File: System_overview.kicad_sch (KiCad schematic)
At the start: 0 parts

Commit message: creating hierarchy
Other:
- note added: "END OF TRAVEL SWITCHES"
- note removed: "END OF TRAVEL"
- note removed: "EXTERNAL EQUIPMENT"
- note removed: "EXTERNAL LOAD / MECHANICS"
- note removed: "LOWER"
- note removed: "NO / NC and wiring: TBD"
- note removed: "Reed contacts"
- note removed: "Shared return shown"
- note removed: "UPPER"
- note removed: "Upper / lower reed switches"
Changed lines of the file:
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@@
 		)
 	)
-	(polyline
-		(pts
-			(xy 49.82 131.14) (xy 57.82 131.14) (xy 57.82 115.98) (xy 109.82 115.98)
-		)
-		(stroke
-			(width 0.25)
-			(type default)
-		)
-		(fill
-			(type none)
-		)
-	)
-	(polyline
-		(pts
-			(xy 23.82 128.14) (xy 45.82 128.14) (xy 45.82 134.14) (xy 23.82 134.14) (xy 23.82 128.14)
-		)
-		(stroke
-			(width 0.18)
-			(type default)
-		)
-		(fill
-			(type none)
-		)
-	)
-	(polyline
-		(pts
-			(xy 23.82 141.14) (xy 45.82 141.14) (xy 45.82 147.14) (xy 23.82 147.14) (xy 23.82 141.14)
-		)
-		(stroke
-			(width 0.18)
-			(type default)
-		)
-		(fill
-			(type none)
-		)
-	)
-	(polyline
-		(pts
-			(xy 49.82 144.14) (xy 70.82 144.14) (xy 70.82 126.14) (xy 109.82 126.14)
-		)
-		(stroke
-			(width 0.25)
+	(rectangle
+		(start 38.1 127)
+		(end 63.5 152.4)
+		(stroke
+			(width 0)
 			(type default)
 		)
@@
 	)
 	(rectangle
+		(start 25.4 114.3)
+		(end 76.2 165.1)
+		(stroke
+			(width 0)
+			(type dash)
+		)
+		(fill
+			(type none)
+		)
+	)
+	(rectangle
 		(start 223.52 154.94)
 		(end 224.79 160.02)
@@
 		)
 	)
-	(polyline
-		(pts
-			(xy 18.82 131.14) (xy 18.82 152.14) (xy 64.82 152.14) (xy 64.82 136.3) (xy 109.82 136.3)
-		)
-		(stroke
-			(width 0.25)
-			(type default)
-		)
-		(fill
-			(type none)
-		)
-	)
 	(rectangle
 		(start 257.81 154.94)
@@
 		)
 	)
-	(polyline
-		(pts
-			(xy 14.82 109.14) (xy 76.82 109.14) (xy 76.82 158.14) (xy 14.82 158.14) (xy 14.82 109.14)
-		)
-		(stroke
-			(width 0.25)
-			(type dash)
-		)
-		(fill
-			(type none)
-		)
-	)
 	(rectangle
 		(start 38.1 63.5)
@@
 		)
 	)
-	(polyline
-		(pts
-			(xy 241.3 90.17) (xy 241.3 95.25)
-		)
-		(stroke
-			(width 0.254)
-			(type solid)
-			(color 0 0 0 1)
-		)
-		(fill
-			(type none)
-		)
-	)
 	(rectangle
 		(start 215.9 139.7)
@@
 		)
 	)
-	(text "END OF TRAVEL"
-		(exclude_from_sim no)
-		(at 18.82 115.14 0)
-		(effects
-			(font
-				(size 1.6 1.6)
-				(bold yes)
-			)
-			(justify left)
-		)
-	)
 	(text "DESK MECHANISM"
 		(exclude_from_sim no)
@@
 		)
 	)
-	(text "UPPER"
-		(exclude_from_sim no)
-		(at 24.82 137.14 0)
-		(effects
-			(font
-				(size 1 1)
-			)
-			(justify left)
-		)
-	)
 	(text "19.5 V, 3 A"
 		(exclude_from_sim no)
@@
 		)
 	)
-	(text "NO / NC and wiring: TBD"
-		(exclude_from_sim no)
-		(at 20.82 155.14 0)
-		(effects
-			(font
-				(size 1.05 1.05)
-			)
-			(justify left)
-		)
-	)
 	(text "Control input / logic"
 		(exclude_from_sim no)
@@
 		)
 	)
-	(text "LOWER"
-		(exclude_from_sim no)
-		(at 24.82 150.14 0)
-		(effects
-			(font
-				(size 1 1)
-			)
-			(justify left)
-		)
-	)
 	(text "DC POWER SUPPLY"
 		(exclude_from_sim no)
@@
 		)
 	)
-	(text "EXTERNAL EQUIPMENT"
-		(exclude_from_sim no)
-		(at 14.82 42.14 0)
-		(effects
-			(font
-				(size 1.5 1.5)
-				(bold yes)
-			)
-			(justify left)
-		)
-	)
-	(text "Reed contacts"
-		(exclude_from_sim no)
-		(at 80.82 109.14 0)
-		(effects
-			(font
-				(size 1.15 1.15)
-			)
-			(justify left)
-		)
-	)
-	(text "EXTERNAL LOAD / MECHANICS"
-		(exclude_from_sim no)
-		(at 217.82 42.14 0)
-		(effects
-			(font
-				(size 1.5 1.5)
-				(bold yes)
-			)
-			(justify left)
-		)
-	)
-	(text "Shared return shown"
-		(exclude_from_sim no)
-		(at 79.82 143.14 0)
-		(effects
-			(font
-				(size 1 1)
-			)
-			(justify left)
+	(text "END OF TRAVEL SWITCHES"
+		(exclude_from_sim no)
+		(at 26.035 115.57 0)
+		(effects
+			(font
+				(size 1.524 1.524)
+				(thickness 0.1905)
+			)
+			(justify left top)
 		)
 	)
@@
 			(font
 				(size 1.016 1.016)
-			)
-			(justify left)
-		)
-	)
-	(text "Upper / lower reed switches"
-		(exclude_from_sim no)
-		(at 18.82 121.14 0)
-		(effects
-			(font
-				(size 1.2 1.2)
 			)
 			(justify left)
@@
 	(polyline
 		(pts
-			(xy 18.82 144.14) (xy 28.82 144.14)
-		)
-		(stroke
-			(width 0.25)
-			(type default)
-		)
-	)
-	(polyline
-		(pts
-			(xy 28.82 131.14) (xy 38.82 129.64)
-		)
-		(stroke
-			(width 0.25)
-			(type default)
+			(xy 104.14 116.84) (xy 114.3 116.84)
+		)
+		(stroke
+			(width 0)
+			(type solid)
+			(color 0 0 0 1)
+		)
+	)
+	(polyline
+		(pts
+			(xy 63.5 134.62) (xy 99.06 134.62)
+		)
+		(stroke
+			(width 0)
+			(type solid)
+			(color 0 0 0 1)
 		)
 	)
@@
 	(polyline
 		(pts
-			(xy 18.82 131.14) (xy 28.82 131.14)
-		)
-		(stroke
-			(width 0.25)
-			(type default)
-		)
-	)
-	(polyline
-		(pts
 			(xy 262.89 154.94) (xy 264.16 153.67)
 		)
@@
 	(polyline
 		(pts
-			(xy 39.82 144.14) (xy 49.82 144.14)
-		)
-		(stroke
-			(width 0.25)
-			(type default)
+			(xy 63.5 139.7) (xy 104.14 139.7)
+		)
+		(stroke
+			(width 0)
+			(type solid)
+			(color 0 0 0 1)
+		)
+	)
+	(polyline
+		(pts
+			(xy 99.06 134.62) (xy 99.06 111.76)
+		)
+		(stroke
+			(width 0)
+			(type solid)
+			(color 0 0 0 1)
 		)
 	)
@@
 	(polyline
 		(pts
+			(xy 104.14 139.7) (xy 104.14 116.84)
+		)
+		(stroke
+			(width 0)
+			(type solid)
+			(color 0 0 0 1)
+		)
+	)
+	(polyline
+		(pts
 			(xy 262.89 154.94) (xy 269.24 154.94)
 		)
@@
 	(polyline
 		(pts
+			(xy 101.6 137.16) (xy 101.6 114.3)
+		)
+		(stroke
+			(width 0)
+			(type solid)
+			(color 0 0 0 1)
+		)
+	)
+	(polyline
+		(pts
 			(xy 210.82 78.74) (xy 210.82 100.33)
 		)
@@
 	(polyline
 		(pts
+			(xy 63.5 137.16) (xy 101.6 137.16)
+		)
+		(stroke
+			(width 0)
+			(type solid)
+			(color 0 0 0 1)
+		)
+	)
+	(polyline
+		(pts
 			(xy 220.98 160.02) (xy 227.33 160.02)
 		)
@@
 	(polyline
 		(pts
+			(xy 99.06 111.76) (xy 114.3 111.76)
+		)
+		(stroke
+			(width 0)
+			(type solid)
+			(color 0 0 0 1)
+		)
+	)
+	(polyline
+		(pts
 			(xy 262.89 77.47) (xy 269.24 77.47)
 		)
@@
 	(polyline
 		(pts
-			(xy 18.82 144.14) (xy 18.82 152.14)
-		)
-		(stroke
-			(width 0.25)
-			(type default)
-		)
-	)
-	(polyline
-		(pts
 			(xy 177.8 100.33) (xy 210.82 100.33)
 		)
@@
 	(polyline
 		(pts
-			(xy 39.82 131.14) (xy 49.82 131.14)
-		)
-		(stroke
-			(width 0.25)
-			(type default)
-		)
-	)
-	(polyline
-		(pts
 			(xy 262.89 154.94) (xy 264.16 156.21)
 		)
@@
 	(polyline
 		(pts
+			(xy 101.6 114.3) (xy 114.3 114.3)
+		)
+		(stroke
+			(width 0)
+			(type solid)
+			(color 0 0 0 1)
+		)
+	)
+	(polyline
+		(pts
 			(xy 177.8 105.41) (xy 228.6 105.41)
 		)
@@
 	(polyline
 		(pts
-			(xy 28.82 144.14) (xy 38.82 142.64)
-		)
-		(stroke
-			(width 0.25)
-			(type default)
-		)
-	)
+			(xy 241.3 90.17) (xy 241.3 95.25)
+		)
+		(stroke
+			(width 0.254)
+			(type solid)
+			(color 0 0 0 1)
+		)
+	)

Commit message: testing links
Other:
- note added: "Return to front sheet"
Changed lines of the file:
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@@
+		)
+	)
+	(text "Return to front sheet"
+		(exclude_from_sim no)
+		(at 12.7 197.485 0)
+		(effects
+			(font
+				(face "DejaVu Sans")
+				(size 2.032 2.032)
+				(thickness 0.3175)
+				(color 0 0 0 1)
+			)
+			(justify left bottom)
+			(href "#1")
 		)
 	)

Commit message: system overview and interfaces done
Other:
- sheet Block_diagram renamed Block diagram
- added sheet DC power supply (Interface_Power_supply.kicad_sch)
- added sheet Limit switches (Interface_Limit_switches.kicad_sch)
- added sheet Servomotor (Interface_servomotor.kicad_sch)
- note added: "${SHEETNAME}"
- note added: "Bottom"
- note added: "Control logic HMI Motor driver Encoder interface Limit switch interface"
- note added: "Motor, gearbox and encoder"
- note added: "This sheet shows the overall system and the interfaces to external components. External components are shown for system context only and are not part of this schematic. Only the "DESIGNED SUBSYSTEM" is covered by this schematic."
- note added: "Top"
- note removed: "19.5 V, 3 A"
- note removed: "Control input / logic"
- note removed: "DC POWER SUPPLY"
- note removed: "END OF TRAVEL SWITCHES"
- note removed: "Encoder GND"
- note removed: "Encoder decoding"
- note removed: "Encoder signal A"
- note removed: "Encoder signal B"
- note removed: "Encoder supply"
- note removed: "End-switch inputs"
- note removed: "GND"
- note removed: "Integrated encoder"
- note removed: "Motor / gearbox"
- note removed: "Motor A"
- note removed: "Motor B"
- note removed: "Motor power stage"
- note removed: "S24"
- note removed: "SERVOMOTOR PACKAGE"
- note removed: "STANDING DESK / SYSTEM OVERVIEW"

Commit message: testing green mask
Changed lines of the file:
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@@
 			(width 0)
 			(type dash)
+			(color 0 0 0 1)
 		)
 		(fill
@@
 	(text "This sheet shows the overall system and the interfaces to external components.\nExternal components are shown for system context only and are not part of this schematic.\nOnly the \"DESIGNED SUBSYSTEM\" is covered by this schematic."
 		(exclude_from_sim no)
-		(at 25.4 165.1 0)
+		(at 38.1 166.37 0)
 		(effects
 			(font
-				(size 1.27 1.27)
+				(size 2.032 2.032)
+				(color 194 0 0 1)
 			)
 			(justify left top)
@@
 			(font
 				(size 1.27 1.27)
+				(color 0 0 0 1)
 			)
 		)
@@
 				(size 1.524 1.524)
 				(thickness 0.1905)
+				(bold yes)
+				(color 255 0 0 1)
 			)
 			(justify left top)
@@
 	(text "${SHEETNAME}"
 		(exclude_from_sim no)
-		(at 283.21 13.97 0)
+		(at 283.21 14.605 0)
 		(effects
 			(font
-				(size 2.54 2.54)
+				(face "DejaVu Sans")
+				(size 3.81 3.81)
 				(bold yes)
+				(color 0 0 0 1)
 			)
 			(justify right top)

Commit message: reorganised sch and pcb
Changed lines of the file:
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@@
 			(font
 				(size 2.032 2.032)
-				(color 194 0 0 1)
+				(color 0 0 0 1)
 			)
 			(justify left top)
@@
 		(effects
 			(font
-				(size 1.27 1.27)
+				(size 1.524 1.524)
 				(color 0 0 0 1)
 			)
@@
 	(text "DESIGNED SUBSYSTEM"
 		(exclude_from_sim no)
-		(at 128.27 40.005 0)
+		(at 151.765 42.545 0)
 		(effects
 			(font
 				(face "DejaVu Sans")
-				(size 1.524 1.524)
+				(size 2.032 2.032)
 				(thickness 0.1905)
 				(bold yes)
-				(color 255 0 0 1)
-			)
-			(justify left top)
+				(color 0 0 0 1)
+			)
+			(justify top)
 		)
 	)
@@
 		)
 		(fill
-			(color 194 194 194 1)
+			(color 250 240 240 1)
 		)
 		(property "Sheetname" "Servomotor"
@@
 		)
 		(fill
-			(color 194 194 194 1)
+			(color 250 240 240 1)
 		)
 		(property "Sheetname" "DC power supply"
@@
 		)
 		(fill
-			(color 194 194 194 1)
+			(color 250 240 240 1)
 		)
 		(property "Sheetname" "Limit switches"

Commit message: updated sch template (A4)
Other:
- note removed: "${SHEETNAME}"
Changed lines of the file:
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@@
-		)
-	)
-	(text "${SHEETNAME}"
-		(exclude_from_sim no)
-		(at 283.21 14.605 0)
-		(effects
-			(font
-				(face "DejaVu Sans")
-				(size 3.81 3.81)
-				(bold yes)
-				(color 0 0 0 1)
-			)
-			(justify right top)
 		)
 	)
@@
 				(size 2.032 2.032)
 				(thickness 0.3175)
-				(color 0 0 0 1)
+				(color 0 0 194 1)
 			)
 			(justify left bottom)

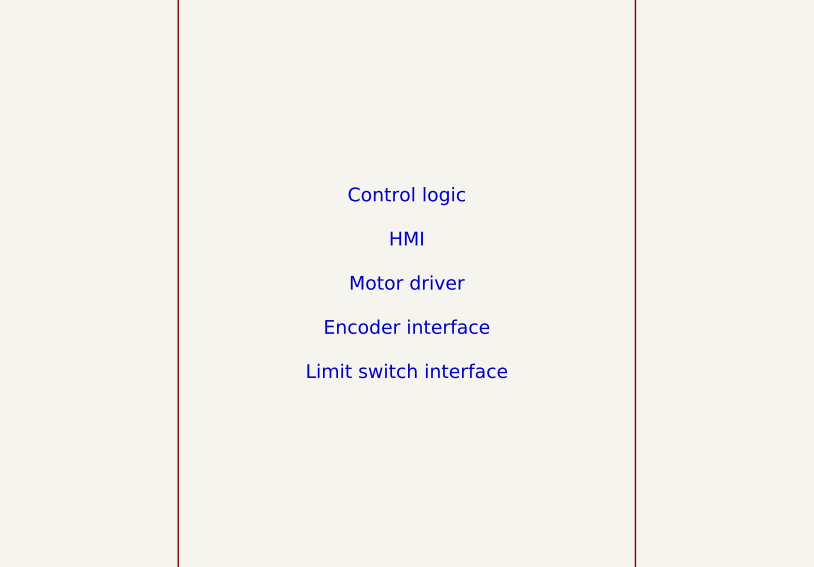
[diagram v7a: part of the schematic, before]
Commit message: new sch size
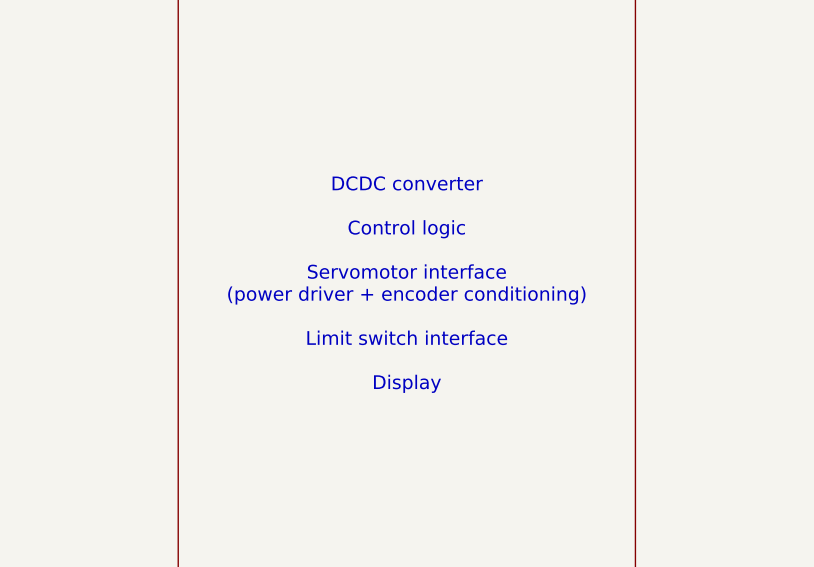
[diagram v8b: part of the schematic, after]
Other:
- note added: "DCDC converter Control logic Servomotor interface (power driver + encoder conditioning) Limit switch interface Display"
- note removed: "Control logic HMI Motor driver Encoder interface Limit switch interface"
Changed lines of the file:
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@@
 		)
 	)
-	(text "Control logic\n\nHMI\n\nMotor driver\n\nEncoder interface\n\nLimit switch interface"
+	(text "DCDC converter\n\nControl logic\n\nServomotor interface\n(power driver + encoder conditioning)\n\nLimit switch interface\n\nDisplay"
 		(exclude_from_sim no)
 		(at 152.4 86.36 0)
